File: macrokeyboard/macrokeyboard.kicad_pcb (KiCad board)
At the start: 4 copper layers, 145 x 85 mm, 135 parts, among them J1 USB_C_Receptacle_USB2.0_16P, J2 Conn_01x02_MountingPin, J3 Conn_02x04_Odd_Even, J4 Conn_01x03, J5 Conn_01x03, J6 Conn_01x02, Q1 Si1308EDL, SW1 SW_SPDT, SW2 SW_SPDT, SW3 SW_Push, SW4 SW_Push, SW5 SW_Push, SW6 SW_Push, U1 STM32F072VBTx, U2 nRF52810-QCxx, U3 BQ25186DLHR, U4 RV-3028-C7, U5 E-INK_Display_Conn, U6 TPS7A0233DBVR, U7 TPS7A0233DBVR, Y1 32.768KHz, Y2 32MHz

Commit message: important changes before order
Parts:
- removed D15, D16: 1N4148WS, Diode_SMD:D_SOD-323
- removed SW1, SW2: SW_SPDT, 1_macrokeys:SK12D07VG4
- added D3: 1N4148W, Diode_SMD:D_SOD-123, F.Cu at (102.6, 76.0)
- added D4: 1N4148W, Diode_SMD:D_SOD-123, F.Cu at (121.7, 76.0)
- added U8: SK12D07VG4, 1_macrokeys:SK12D07VG4, F.Cu at (157.9, 49.2)
- added U9: SK12D07VG4, 1_macrokeys:SK12D07VG4, F.Cu at (169.2, 49.2)
- D1, D10, D11, D12, D13, D14, D2, D5, D6, D7, D8, D9: value 1N4148WS -> 1N4148W; footprint Diode_SMD:D_SOD-323 -> Diode_SMD:D_SOD-123
- moved D8 42.6 mm to (121.6, 95.1)
- moved D11 42.6 mm to (102.5, 114.1)
- moved D7 42.6 mm to (102.5, 95.1)
- moved D12 42.5 mm to (121.6, 113.9)
- moved D13 38.2 mm to (140.8, 114.1)
- moved D10 38.2 mm to (159.8, 95.0)
- moved D14 38.2 mm to (159.8, 113.9)
- moved D9 38.1 mm to (140.7, 95.1)
- moved D6 38.1 mm to (159.6, 76.0)
- moved D5 38.0 mm to (140.5, 75.9)
- moved R20 4.23 mm to (156.5, 52.4), turned to 180 degrees
- moved R18 2.29 mm to (159.7, 52.4), turned to 0 degrees
- moved R7 1.25 mm to (164.2, 94.9)
- moved R8 0.97 mm to (163.9, 114.1)
- moved R6 0.88 mm to (163.7, 75.9)
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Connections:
- D11 pad 1: /ROW3 -> /ROW4
- D12 pad 1: /ROW3 -> /ROW4
- D7 pad 1: /ROW2 -> /ROW3
- D8 pad 1: /ROW2 -> /ROW3
- S10 pad 2: Net-(D10-A) -> Net-(D8-A)
- S11 pad 2: Net-(D11-A) -> Net-(D9-A)
- S12 pad 2: Net-(D12-A) -> Net-(D10-A)
- S13 pad 2: Net-(D13-A) -> Net-(D11-A)
- S14 pad 2: Net-(D14-A) -> Net-(D12-A)
- S15 pad 2: Net-(D15-A) -> Net-(D13-A)
- S16 pad 2: Net-(D16-A) -> Net-(D14-A)
- S5 pad 2: Net-(D5-A) -> Net-(D3-A)
- S6 pad 2: Net-(D6-A) -> Net-(D4-A)
- S7 pad 2: Net-(D7-A) -> Net-(D5-A)
- S8 pad 2: Net-(D8-A) -> Net-(D6-A)
- S9 pad 2: Net-(D9-A) -> Net-(D7-A)
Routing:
- net Net-(U1-PC11): track 0.00 -> 32.5 mm
- net Net-(U1-PC10): track 0.00 -> 31.2 mm
- net +5V: track 39.1 -> 60.8 mm, vias 1 -> 2
- net Net-(D15-A): track 10.2 -> 0.00 mm
- net Net-(D16-A): track 10.2 -> 0.00 mm
- net Net-(D3-A): track 0.00 -> 9.74 mm
- net Net-(D4-A): track 0.00 -> 9.73 mm
- net Net-(R16-Pad2): track 0.00 -> 3.48 mm
- net /ROW1: track 80.9 -> 82.1 mm
- net Net-(D5-A): track 10.2 -> 9.59 mm
- net Net-(D8-A): track 10.2 -> 9.61 mm
- net Net-(D2-A): track 10.2 -> 9.65 mm
- net Net-(D1-A): track 10.2 -> 9.65 mm
- net Net-(D7-A): track 10.2 -> 9.65 mm
- net Net-(D11-A): track 10.2 -> 9.66 mm
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
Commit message: PCB completion
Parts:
- removed NT1: NetTie_2, NetTie:NetTie-2_SMD_Pad0.5mm
- added C41: 1.5pF, Capacitor_SMD:C_0402_1005Metric, F.Cu at (0.00, 0.00)
- added J7: Chip_ant, 1_macrokeys:KH5220-A36, F.Cu at (0.00, 0.00)
- added L3: 4.3nH, Inductor_SMD:L_0402_1005Metric, F.Cu at (0.00, 0.00)
- C1, C12, C2, C25, C3, C4, C5, C6, C7, C8, C9, R11, R12, U4: moved to F.Cu
- moved R14 254.8 mm to (0.00, 0.00)
- moved TH1 253.9 mm to (0.00, 0.00), turned to 0 degrees
- moved TH2 253.1 mm to (0.00, 0.00), turned to 0 degrees
- moved R13 252.3 mm to (0.00, 0.00)
- moved C18 229.9 mm to (0.00, 0.00), turned to 0 degrees
- moved R15 229.2 mm to (0.00, 0.00), turned to 0 degrees
- moved C17 228.4 mm to (0.00, 0.00), turned to 0 degrees
- moved C37 228.3 mm to (0.00, 0.00), turned to 0 degrees
- moved C22 227.9 mm to (0.00, 0.00), turned to 0 degrees
- moved C20 227.9 mm to (0.00, 0.00), turned to 0 degrees
- moved R26 227.3 mm to (0.00, 0.00), turned to 0 degrees
- moved Q1 226.9 mm to (0.00, 0.00), turned to 0 degrees
- moved L2 226.9 mm to (0.00, 0.00), turned to 0 degrees
- moved C16 226.7 mm to (0.00, 0.00), turned to 0 degrees
- moved D17 226.7 mm to (0.00, 0.00), turned to 0 degrees
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- renumbered U8 to BLUE/USB, U9 to PWR
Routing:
- net +3V3: track 66.9 -> 60.7 mm, vias 18 -> 20
- net /MCU/I2C1_SDA: track 75.9 -> 70.2 mm, vias 2 -> 3
- net /MCU/PWR_EN: track 37.9 -> 42.7 mm, vias 2 -> 3
- net /Bluetooth/NRF-CS: track 21.4 -> 26.2 mm
- net /Bluetooth/NRF-MOSI: track 24.1 -> 28.3 mm
- net /Bluetooth/NRF-MISO: track 23.6 -> 27.6 mm
- net /Bluetooth/NRF-SCLK: track 23.0 -> 26.9 mm
- net Net-(J7-In): track 0.00 -> 3.75 mm
- net GND: track 15.6 -> 18.1 mm, vias 11 -> 214
- net Net-(J5-Pin_3): track 5.88 -> 3.54 mm
- net /MCU/I2C1_SCL: track 73.6 -> 71.5 mm, vias 2 -> 4
- net /MCU/SWCLK: track 3.89 -> 1.91 mm
- net /MCU/POT0: track 52.9 -> 54.9 mm
- net +5V: track 60.8 -> 59.0 mm, vias 2 -> 3
- net /MCU/POT1: track 36.5 -> 38.4 mm
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- removed copper zone on F.Cu, net /Bluetooth/ANT
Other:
- outline, holes or cut-outs redrawn
- board text added: "Author: Abdelrahman Elbarkouky Date of Completion: 12/10/2026"

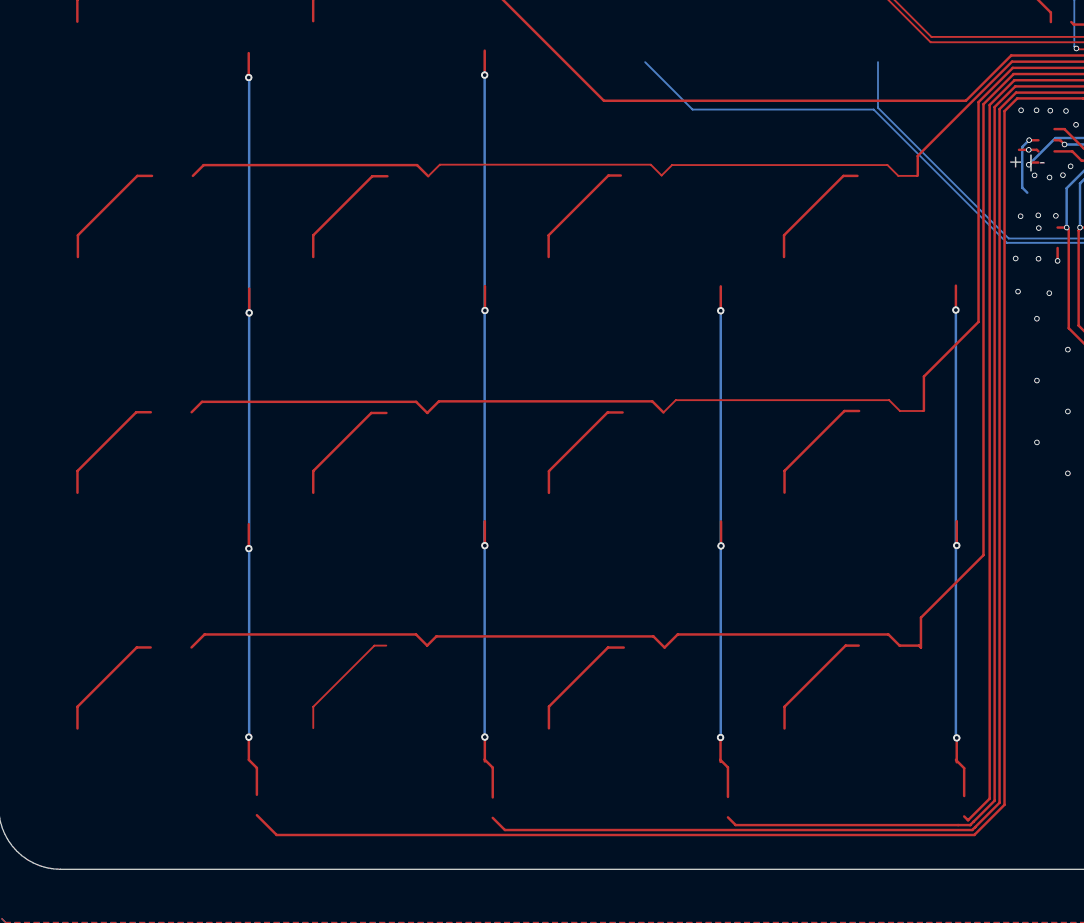
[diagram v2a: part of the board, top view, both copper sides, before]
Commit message: added production files and BOM
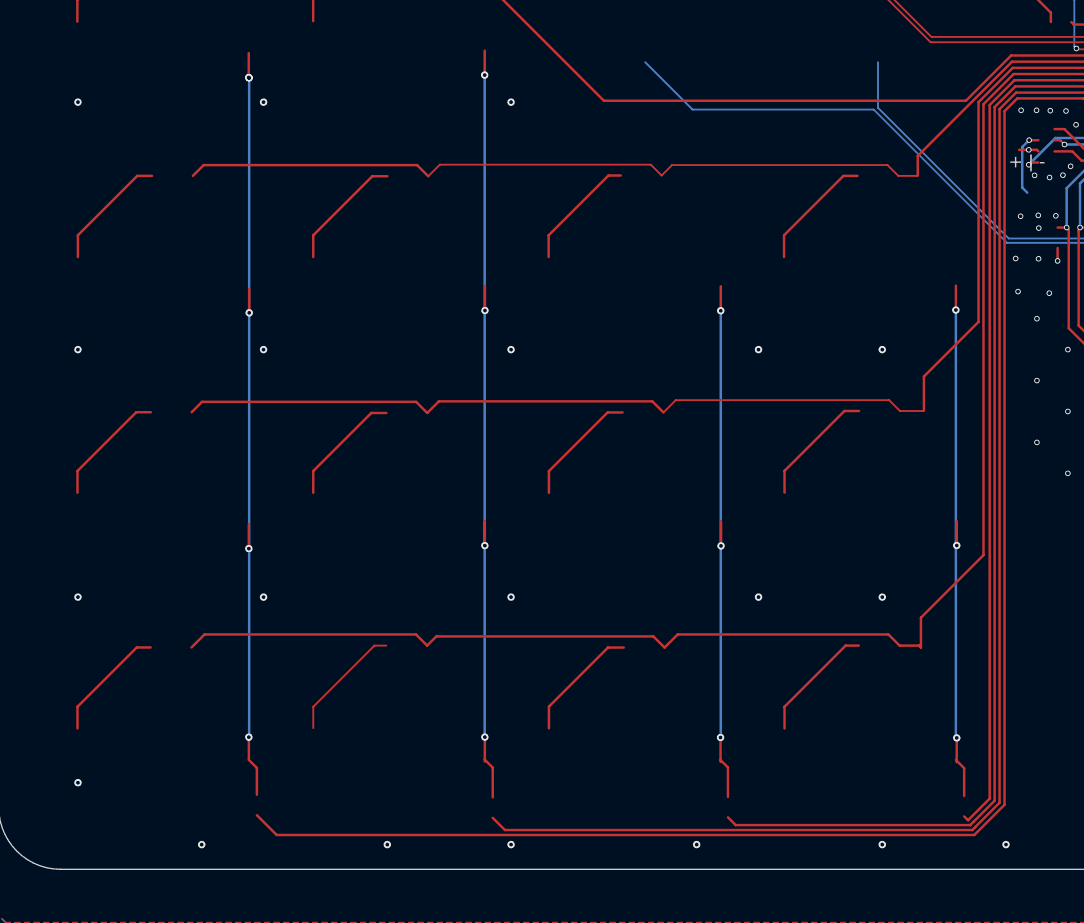
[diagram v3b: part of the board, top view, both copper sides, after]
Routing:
- net Net-(R1-Pad1): vias 4 -> 5
- net GND: vias 214 -> 234
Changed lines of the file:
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@@
 		(capping no)
 		(filling no)
-		(zone_defaults)
 		(pcbplotparams
 			(layerselection 0x00000000_00000000_55555555_5755f5ff)
@@
 	)
 	(via
+		(at 110 90)
+		(size 0.6)
+		(drill 0.3)
+		(layers "F.Cu" "B.Cu")
+		(free yes)
+		(net "GND")
+	)
+	(via
 		(at 212.5 57.5)
 		(size 0.45)
@@
 	)
 	(via
+		(at 150 110)
+		(size 0.6)
+		(drill 0.3)
+		(layers "F.Cu" "B.Cu")
+		(free yes)
+		(net "GND")
+	)
+	(via
 		(at 191 66)
 		(size 0.6)
@@
 	)
 	(via
+		(at 95 110)
+		(size 0.6)
+		(drill 0.3)
+		(layers "F.Cu" "B.Cu")
+		(free yes)
+		(net "GND")
+	)
+	(via
 		(at 92.5 50)
 		(size 0.45)
@@
 	)
 	(via
+		(at 160 130)
+		(size 0.6)
+		(drill 0.3)
+		(layers "F.Cu" "B.Cu")
+		(free yes)
+		(net "GND")
+	)
+	(via
 		(at 177.5 92.5)
 		(size 0.45)
@@
 	)
 	(via
+		(at 130 90)
+		(size 0.6)
+		(drill 0.3)
+		(layers "F.Cu" "B.Cu")
+		(free yes)
+		(net "GND")
+	)
+	(via
 		(at 220.05796 71.44)
 		(size 0.45)
@@
 	)
 	(via
+		(at 105 130)
+		(size 0.6)
+		(drill 0.3)
+		(layers "F.Cu" "B.Cu")
+		(free yes)
+		(net "GND")
+	)
+	(via
 		(at 182.5 100)
 		(size 0.45)
@@
 	)
 	(via
+		(at 170 130)
+		(size 0.6)
+		(drill 0.3)
+		(layers "F.Cu" "B.Cu")
+		(free yes)
+		(net "GND")
+	)
+	(via
 		(at 181 64)
 		(size 0.6)
@@
 	)
 	(via
+		(at 130 130)
+		(size 0.6)
+		(drill 0.3)
+		(layers "F.Cu" "B.Cu")
+		(free yes)
+		(net "GND")
+	)
+	(via
 		(at 220.95 67.6)
 		(size 0.45)
@@
 	)
 	(via
+		(at 110 70)
+		(size 0.6)
+		(drill 0.3)
+		(layers "F.Cu" "B.Cu")
+		(free yes)
+		(net "GND")
+	)
+	(via
 		(at 218.930201 69.95)
 		(size 0.45)
@@
 	)
 	(via
+		(at 160 110)
+		(size 0.6)
+		(drill 0.3)
+		(layers "F.Cu" "B.Cu")
+		(free yes)
+		(net "GND")
+	)
+	(via
 		(at 217.25 71.191)
 		(size 0.45)
@@
 	)
 	(via
+		(at 150 90)
+		(size 0.6)
+		(drill 0.3)
+		(layers "F.Cu" "B.Cu")
+		(free yes)
+		(net "GND")
+	)
+	(via
 		(at 177.5 87.5)
 		(size 0.45)
@@
 	)
 	(via
+		(at 130 110)
+		(size 0.6)
+		(drill 0.3)
+		(layers "F.Cu" "B.Cu")
+		(free yes)
+		(net "GND")
+	)
+	(via
 		(at 210 105)
 		(size 0.45)
@@
 	)
 	(via
+		(at 95 125)
+		(size 0.6)
+		(drill 0.3)
+		(layers "F.Cu" "B.Cu")
+		(free yes)
+		(net "GND")
+	)
+	(via
 		(at 100 50)
 		(size 0.45)
@@
 	)
 	(via
+		(at 160 90)
+		(size 0.6)
+		(drill 0.3)
+		(layers "F.Cu" "B.Cu")
+		(free yes)
+		(net "GND")
+	)
+	(via
 		(at 207.5 85)
 		(size 0.45)
@@
 	)
 	(via
+		(at 110 110)
+		(size 0.6)
+		(drill 0.3)
+		(layers "F.Cu" "B.Cu")
+		(free yes)
+		(net "GND")
+	)
+	(via
 		(at 200 85)
 		(size 0.45)
@@
 	)
 	(via
+		(at 95 70)
+		(size 0.6)
+		(drill 0.3)
+		(layers "F.Cu" "B.Cu")
+		(free yes)
+		(net "GND")
+	)
+	(via
 		(at 212.5 95)
 		(size 0.45)
@@
 	)
 	(via
+		(at 95 90)
+		(size 0.6)
+		(drill 0.3)
+		(layers "F.Cu" "B.Cu")
+		(free yes)
+		(net "GND")
+	)
+	(via
 		(at 160 60)
 		(size 0.45)
@@
 	)
 	(via
+		(at 120 130)
+		(size 0.6)
+		(drill 0.3)
+		(layers "F.Cu" "B.Cu")
+		(free yes)
+		(net "GND")
+	)
+	(via
 		(at 210 60)
 		(size 0.45)
@@
 	)
 	(via
+		(at 130 70)
+		(size 0.6)
+		(drill 0.3)
+		(layers "F.Cu" "B.Cu")
+		(free yes)
+		(net "GND")
+	)
+	(via
 		(at 174.6 75.9)
 		(size 0.45)
@@
 	)
 	(via
+		(at 145 130)
+		(size 0.6)
+		(drill 0.3)
+		(layers "F.Cu" "B.Cu")
+		(free yes)
+		(net "GND")
+	)
+	(via
 		(at 172.5 87.5)
 		(size 0.45)
@@
 	)
 	(via
+		(at 108.835785 68.045785)
+		(size 0.6)
+		(drill 0.3)
+		(layers "F.Cu" "B.Cu")
+		(net "Net-(R1-Pad1)")
+	)
+	(via
 		(at 108.81 121.32)
 		(size 0.6)
@@
 		(polygon
 			(pts
-				(xy 226.59 116.11) (xy 226.59 129) (xy 218.641333 129) (xy 217.28 149.419952) (xy 217.28 116.11)
+				(xy 226.59 116.11) (xy 226.59 129) (xy 226.61 131.31) (xy 217.28 131.4) (xy 217.28 116.11)
 			)
 		)

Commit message: fabrication files
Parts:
- removed C34, C40: 1uF, Capacitor_SMD:C_0603_1608Metric
- removed U7: TPS7A0233DBVR, 1_macrokeys:SOT_233DBVR_TEX
- added R29: 10k, Resistor_SMD:R_0603_1608Metric, F.Cu at (0.00, 0.00)
- added REF**: areyousure, 1_macrokeys:areyousure, F.Cu at (0.00, 0.00)
- R19: value 1k -> 4.7k
- R24: value 1k -> 10k
- U6: value TPS7A0233DBVR -> DS8572-33S5
- the big man: renamed from U1
- renumbered BLUE/USB to U8, PWR to U9
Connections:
- D24 pad 1: GND -> Net-(D24-K)
- R24 pad 2: Net-(U3-*PG/GPO) -> +3V3
- U3 pad 3: Net-(U3-*PG/GPO) -> Net-(D24-K)
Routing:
- net Net-(D24-K): track 0.00 -> 27.8 mm, vias 0 -> 2
- net Net-(U3-*PG/GPO): track 21.4 -> 0.00 mm, vias 2 -> 0
- net /MCU/PWR_EN: track 42.7 -> 37.6 mm, vias 3 -> 1
- net Net-(J6-Pin_1): track 5.40 -> 8.35 mm
- net /MCU/State1: track 44.3 -> 41.8 mm
- net +5V: track 59.0 -> 57.1 mm
- net /MCU/BAT-~{CE}: track 22.7 -> 21.5 mm
- net /ROW1: track 81.5 -> 80.8 mm
- net GND: vias 234 -> 244
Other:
- board text added: "+ -"
- board text removed: "+ | -"
